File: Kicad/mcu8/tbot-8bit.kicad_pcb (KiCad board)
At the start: 2 copper layers, 80 x 100 mm, 63 parts, among them IC201 TLV1117-50, IC301 PIC16F1778, IC401 MCP2221A, K201 Battery, K301 MCU 1, K302 ICSP, K303 MCU 2, K401 FRONT #1, K402 FRONT #2, K403 VIN, K404 +5V, K405 FRONT #3, K406 SERVO LEFT, K407 USB/UART, K408 SERVO RIGHT, T201 DMP2305U, T202 DMP2305U

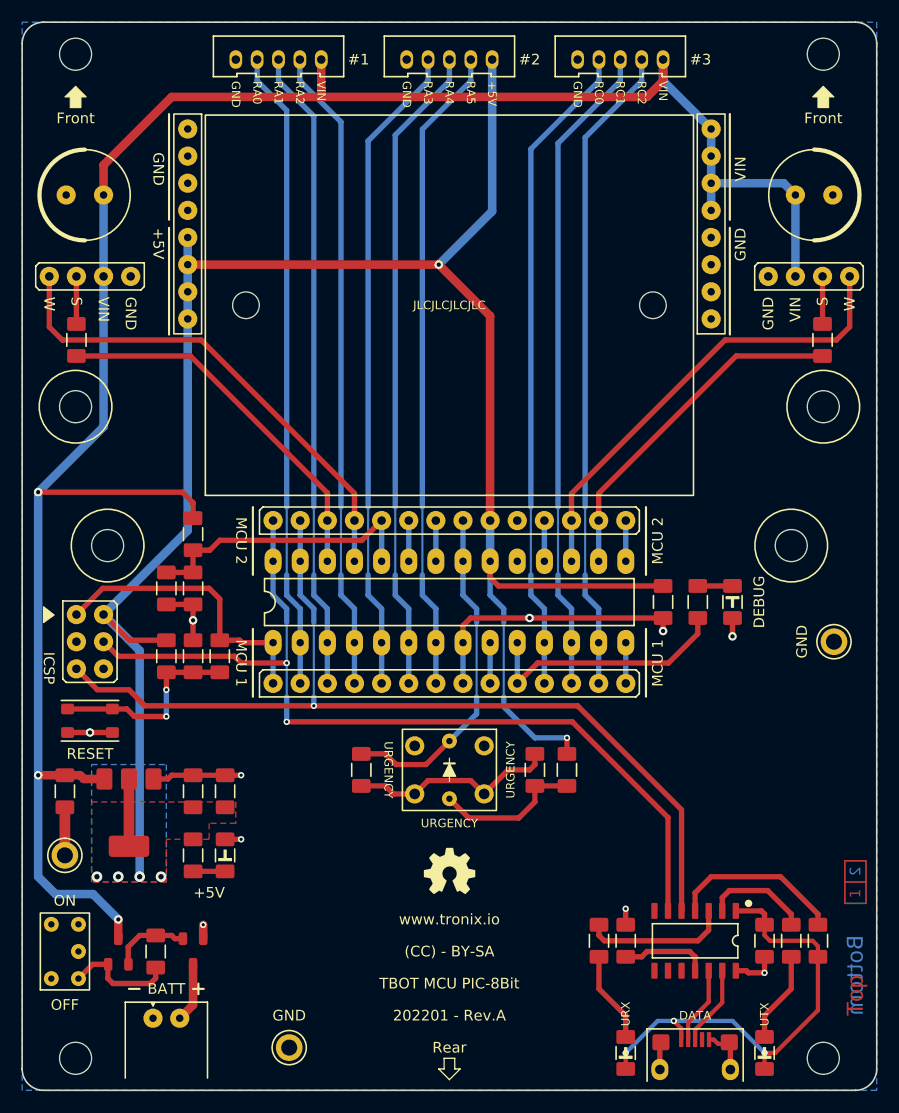
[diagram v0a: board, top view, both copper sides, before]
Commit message: Update MCU 8Bit
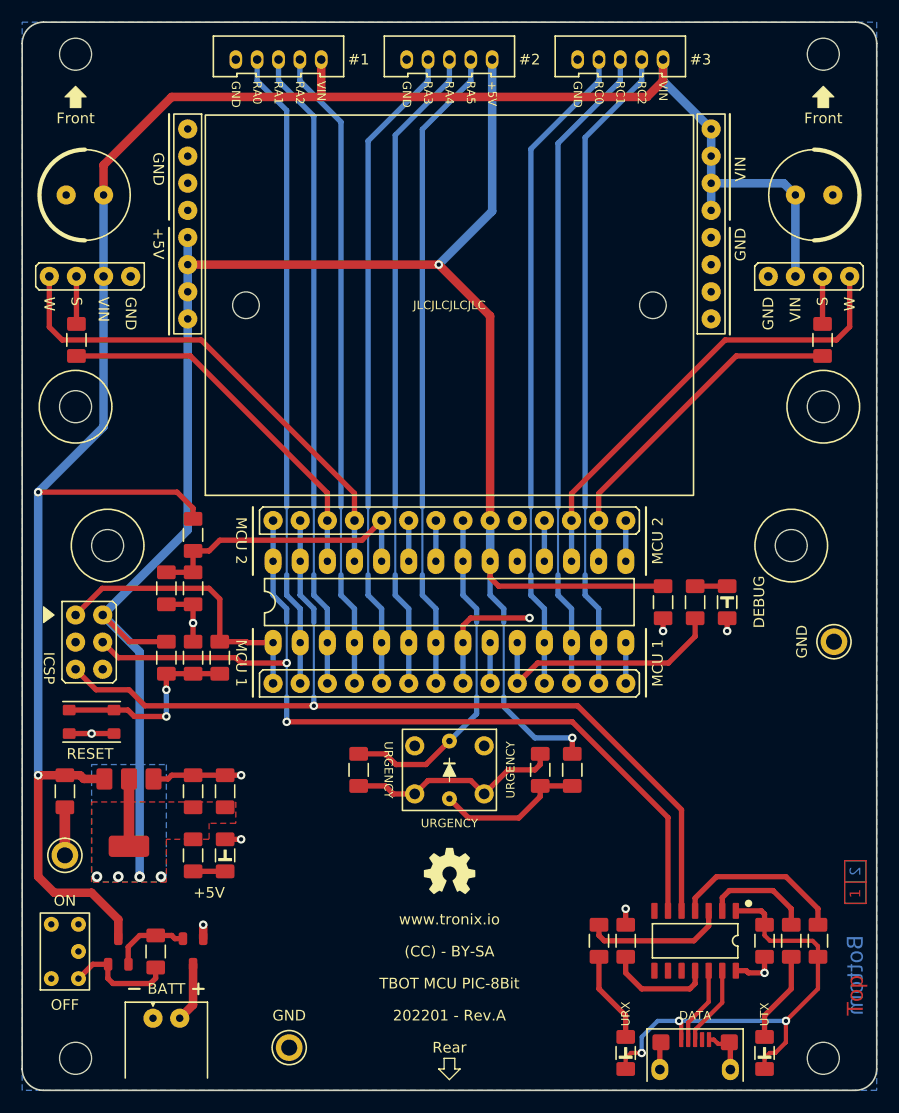
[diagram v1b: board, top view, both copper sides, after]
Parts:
- moved LED401 0.50 mm to (166.0, 104.3)
- moved R401 0.50 mm to (151.5, 120.0)
- moved R402 0.50 mm to (148.5, 120.0)
- moved R404 0.25 mm to (163.0, 104.3)
- moved R403 0.25 mm to (131.5, 120.0)
- moved S301 0.18 mm to (106.5, 115.5)
- moved C301 0.14 mm to (116.0, 109.5)
- moved R301 0.14 mm to (113.5, 109.5)
- moved R302 0.14 mm to (118.5, 109.5)
- moved K302 0.09 mm to (105.0, 105.5)
- moved R203 0.07 mm to (116.0, 98.0)
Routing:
- net GND: track 65.5 -> 52.6 mm
- net Net-(C402-Pad1): track 8.21 -> 10.0 mm
- net Net-(R402-Pad1): track 19.5 -> 20.5 mm
- net VUSB: track 43.4 -> 44.3 mm
- net +5V: track 193.0 -> 193.7 mm
- net /HID/RB0/EMERGENCY: track 31.5 -> 32.0 mm
- net VIN: track 195.9 -> 195.7 mm, vias 3 -> 2

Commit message: Update MCU 8Bit
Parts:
- removed BB401: BREADBOARD-170, tronixio:BREADBOARD-170
- removed C203: 10µ, tronixio:CAPACITOR-1206
- removed C204, C403: 100n, tronixio:CAPACITOR-1206
- removed C401, C404: 220µ/25V, tronixio:CAPACITOR-ELECTROLYTIC-RADIAL-080-115-035
- removed C402: 470n, tronixio:CAPACITOR-1206
- removed IC401: MCP2221A, tronixio:SOIC-SL-14
- removed K401: FRONT #1, tronixio:MOLEX-532530570
- removed K402: FRONT #2, tronixio:MOLEX-532530570
- removed K403: VIN, tronixio:HARWIN-M20-782084x
- removed K404: +5V, tronixio:HARWIN-M20-782084x
- removed K405: FRONT #3, tronixio:MOLEX-532530570
- removed K406: SERVO LEFT, tronixio:HARWIN-M20-999044x
- removed K407: USB/UART, tronixio:FCI-USB-TYPE-B-MICRO-THT
- removed K408: SERVO RIGHT, tronixio:HARWIN-M20-999044x
- removed LED201: Power, tronixio:LED-1206
- removed LED401: Debug, tronixio:LED-1206
- removed LED402: URX, tronixio:LED-1206
- removed LED403: UTX, tronixio:LED-1206
- removed R203: 7K5, tronixio:RESISTOR-1206
- removed R204, R406: 10K, tronixio:RESISTOR-1206
- removed R401, R405, R408: 220Ω, tronixio:RESISTOR-1206
- removed R402: 150Ω, tronixio:RESISTOR-1206
- removed R403: 330Ω, tronixio:RESISTOR-1206
- removed R404, R407, R409: 4K7, tronixio:RESISTOR-1206
- removed S401: EMERGENCY, tronixio:E-SWITCH-TL1240XQ1JXXX
- removed T201, T202: DMP2305U, tronixio:SOT-23-3
- removed TP201, TP202, TP203: GND, tronixio:KEYSTONE-5006
- added BB301: BREADBOARD-170, tronixio:BREADBOARD-170, F.Cu at (140.0, 76.5)
- added C101: 10µ, tronixio:CAPACITOR-1206, F.Cu at (104.0, 122.0)
- added C102: 100n, tronixio:CAPACITOR-1206, F.Cu at (119.0, 122.0)
- added C103: 10µ, tronixio:CAPACITOR-1206, F.Cu at (116.0, 122.0)
- added C104: 100n, tronixio:CAPACITOR-1206, F.Cu at (116.0, 103.0)
- added C303: 100n, tronixio:CAPACITOR-1206, F.Cu at (169.5, 136.0)
- added C304: 220µ/25V, tronixio:CAPACITOR-ELECTROLYTIC-RADIAL-080-115-035, F.Cu at (174.1, 66.2)
- added IC101: TLV1117-50, tronixio:SOT-223-3, F.Cu at (110.0, 124.0)
- added K101: Battery, tronixio:MOLEX-22057025, F.Cu at (112.2, 143.2)
- added K202: ICSP, tronixio:HARWIN-M20-998034x, F.Cu at (105.0, 105.5)
- added K203: MCU 2, tronixio:HARWIN-M20-999144x, F.Cu at (123.5, 96.7)
- added K304: +5V, tronixio:HARWIN-M20-782084x, F.Cu at (115.5, 77.8)
- added K305: FRONT #3, tronixio:MOLEX-532530570, F.Cu at (152.0, 53.5)
- added K306: SERVO LEFT, tronixio:HARWIN-M20-999044x, F.Cu at (110.2, 73.8)
- added K307: USB/UART, tronixio:FCI-USB-TYPE-B-MICRO-THT, F.Cu at (163.0, 147.5)
- added K308: SERVO RIGHT, tronixio:HARWIN-M20-999044x, F.Cu at (169.8, 73.8)
- added LED101: Power, tronixio:LED-1206, F.Cu at (119.0, 128.0)
- added LED301: Debug, tronixio:LED-1206, F.Cu at (166.0, 104.3)
- added LED302: URX, tronixio:LED-1206, F.Cu at (156.5, 146.5)
- added LED303: UTX, tronixio:LED-1206, F.Cu at (169.5, 146.5)
- added R101: 1M, tronixio:RESISTOR-1206, F.Cu at (112.5, 137.0)
- added R102: 4K7, tronixio:RESISTOR-1206, F.Cu at (116.0, 128.0)
- added R103: 7K5, tronixio:RESISTOR-1206, F.Cu at (116.0, 98.0)
- added R104: 10K, tronixio:RESISTOR-1206, F.Cu at (113.5, 103.0)
- added R303: 330Ω, tronixio:RESISTOR-1206, F.Cu at (131.5, 120.0)
- added R304: 4K7, tronixio:RESISTOR-1206, F.Cu at (163.0, 104.3)
- added R305: 220Ω, tronixio:RESISTOR-1206, F.Cu at (105.1, 79.8)
- added R306: 10K, tronixio:RESISTOR-1206, F.Cu at (174.5, 136.0)
- added R307: 4K7, tronixio:RESISTOR-1206, F.Cu at (154.0, 136.0)
- added R308: 220Ω, tronixio:RESISTOR-1206, F.Cu at (174.9, 79.8)
- added R309: 4K7, tronixio:RESISTOR-1206, F.Cu at (172.0, 136.0)
- added S101: Power, tronixio:E-SWITCH-200USPXT1A1M2RE, F.Cu at (104.0, 137.0)
- added T101: DMP2305U, tronixio:SOT-23-3, F.Cu at (116.0, 137.0)
- added T102: DMP2305U, tronixio:SOT-23-3, F.Cu at (109.0, 137.0)
- added TP101: GND, tronixio:KEYSTONE-5006, F.Cu at (104.0, 128.0)
- added TP102: GND, tronixio:KEYSTONE-5006, F.Cu at (125.0, 146.0)
- added TP103: GND, tronixio:KEYSTONE-5006, F.Cu at (176.0, 108.0)
- C201: value 10µ -> 100n
- C301: value 100n -> 220µ/25V; footprint tronixio:CAPACITOR-1206 -> tronixio:CAPACITOR-ELECTROLYTIC-RADIAL-080-115-035
- C302: value 100n -> 470n
- IC201: value TLV1117-50 -> PIC16F1778; footprint tronixio:SOT-223-3 -> tronixio:DIP-28-W762-SOCKET
- IC301: value PIC16F1778 -> MCP2221A; footprint tronixio:DIP-28-W762-SOCKET -> tronixio:SOIC-SL-14
- K201: value Battery -> MCU 1; footprint tronixio:MOLEX-22057025 -> tronixio:HARWIN-M20-999144x
- K301: value MCU 1 -> FRONT #1; footprint tronixio:HARWIN-M20-999144x -> tronixio:MOLEX-532530570
- K302: value ICSP -> FRONT #2; footprint tronixio:HARWIN-M20-998034x -> tronixio:MOLEX-532530570
- K303: value MCU 2 -> VIN; footprint tronixio:HARWIN-M20-999144x -> tronixio:HARWIN-M20-782084x
- R201: value 1M -> 10K
- R202: value 4K7 -> 1K
- R301: value 10K -> 220Ω
- R302: value 1K -> 150Ω
- S201: value Power -> Reset; footprint tronixio:E-SWITCH-200USPXT1A1M2RE -> tronixio:ALPS-SKRPAC
- S301: value Reset -> EMERGENCY; footprint tronixio:ALPS-SKRPAC -> tronixio:E-SWITCH-TL1240XQ1JXXX
- moved K302 60.5 mm to (136.0, 53.5)
- moved K301 58.5 mm to (120.0, 53.5), turned to 0 degrees
- moved K303 55.0 mm to (164.5, 60.0), turned to 0 degrees
- moved IC301 48.4 mm to (163.0, 136.0), turned to -90 degrees
- moved C202 47.4 mm to (160.0, 104.3), turned to -90 degrees
- moved C301 44.5 mm to (105.9, 66.2), turned to 180 degrees
- moved R301 39.4 mm to (151.5, 120.0)
- moved S301 33.8 mm to (140.0, 120.0), turned to 180 degrees
- moved K201 33.3 mm to (123.5, 111.9), turned to 90 degrees
- moved C302 31.9 mm to (156.5, 136.0), turned to 90 degrees
- moved R302 31.8 mm to (148.5, 120.0)
- moved R201 27.5 mm to (113.5, 109.5)
- moved S201 21.6 mm to (106.5, 115.5)
- moved IC201 20.9 mm to (123.5, 108.1), turned to 90 degrees
- moved R202 18.7 mm to (118.5, 109.5), turned to -90 degrees
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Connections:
- C201 pad 1: VIN -> Net-(C201-Pad1)
- C301 pad 1: Net-(C301-Pad1) -> VIN
- C302 pad 1: +5V -> Net-(C302-Pad1)
- IC201 pad 1: GND -> ~{MCLR}
- IC201 pad 2: +5V -> /HID/RA0
- IC201 pad 3: VIN -> /HID/RA1
- IC301 pad 1: ~{MCLR} -> VUSB
- IC301 pad 10: /HID/RA6/LED -> unconnected-(IC301-Pad10)
- IC301 pad 11: /HID/RC0 -> Net-(C302-Pad1)
- IC301 pad 12: /HID/RC1 -> /HID/D-
- IC301 pad 13: /HID/RC2 -> /HID/D+
- IC301 pad 14: RC3 -> GND
- IC301 pad 2: /HID/RA0 -> Net-(IC301-Pad2)
- IC301 pad 3: /HID/RA1 -> Net-(IC301-Pad3)
- IC301 pad 4: /HID/RA2 -> Net-(IC301-Pad4)
- IC301 pad 5: /HID/RA3 -> /HID/RB6/PGC/UTX
- IC301 pad 6: /HID/RA4 -> /HID/RB7/PGD/URX
- IC301 pad 7: /HID/RA5 -> unconnected-(IC301-Pad7)
- IC301 pad 8: GND -> unconnected-(IC301-Pad8)
- IC301 pad 9: RA7 -> unconnected-(IC301-Pad9)
- K201 pad 1: GND -> ~{MCLR}
- K201 pad 2: VBAT -> /HID/RA0
- K301 pad 1: ~{MCLR} -> VIN
- K301 pad 2: /HID/RA0 -> /HID/RA2
- K301 pad 4: /HID/RA2 -> /HID/RA0
- K301 pad 5: /HID/RA3 -> GND
- K302 pad 1: ~{MCLR} -> +5V
- K302 pad 2: +5V -> /HID/RA5
- K302 pad 3: GND -> /HID/RA4
- K302 pad 4: /HID/RB7/PGD/URX -> /HID/RA3
- K302 pad 5: /HID/RB6/PGC/UTX -> GND
- K303 pad 1: /HID/RB7/PGD/URX -> VIN
- K303 pad 2: /HID/RB6/PGC/UTX -> VIN
- K303 pad 3: /HID/RB5/SERVO_L -> VIN
- K303 pad 4: /HID/RB4/WHEEL_L -> VIN
- K303 pad 5: /MCU/RB3/BATTERY_SENSE -> GND
- K303 pad 6: RB2 -> GND
- K303 pad 7: RB1 -> GND
- K303 pad 8: /HID/RB0/EMERGENCY -> GND
- R201 pad 1: Net-(R201-Pad1) -> Net-(C201-Pad1)
- R201 pad 2: Net-(R201-Pad2) -> +5V
- R202 pad 1: Net-(LED201-Pad2) -> ~{MCLR}
- R202 pad 2: +5V -> Net-(C201-Pad1)
- R301 pad 1: Net-(C301-Pad1) -> Net-(R301-Pad1)
- R302 pad 1: ~{MCLR} -> Net-(R302-Pad1)
- R302 pad 2: Net-(C301-Pad1) -> Net-(R301-Pad1)
- S201 pad 1: unconnected-(S201-Pad1) -> GND
- S201 pad 3: Net-(R201-Pad1) -> Net-(C201-Pad1)
- S201 pad 4: (no net) -> Net-(C201-Pad1)
- S301 pad 3: Net-(C301-Pad1) -> Net-(R302-Pad1)
- S301 pad 4: Net-(C301-Pad1) -> Net-(R302-Pad1)
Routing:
- net RB3/BATTERY_SENSE: track 0.00 -> 27.1 mm
- net /MCU/RB3/BATTERY_SENSE: track 27.1 -> 0.00 mm
- net Net-(R402-Pad1): track 20.5 -> 0.00 mm
- net Net-(R302-Pad1): track 0.00 -> 20.5 mm
- net Net-(C301-Pad1): track 18.3 -> 0.00 mm, vias 2 -> 0
- net Net-(C201-Pad1): track 0.00 -> 18.3 mm, vias 0 -> 2
- net Net-(IC401-Pad4): track 16.3 -> 0.00 mm
- net Net-(IC301-Pad4): track 0.00 -> 16.3 mm
- net Net-(R401-Pad1): track 14.1 -> 0.00 mm
- net Net-(R301-Pad1): track 0.00 -> 14.1 mm
- net Net-(IC401-Pad3): track 13.5 -> 0.00 mm
- net Net-(IC301-Pad3): track 0.00 -> 13.5 mm
- net Net-(R201-Pad1): track 10.5 -> 0.00 mm
- net Net-(R101-Pad1): track 0.00 -> 10.5 mm
- net Net-(IC401-Pad2): track 10.2 -> 0.00 mm
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
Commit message: Update tbot-8bit.kicad_pcb
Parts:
- removed TP103: GND, tronixio:KEYSTONE-5006
- moved TP102 54.4 mm to (176.0, 127.0)
- moved TP101 28.0 mm to (125.0, 146.5), turned to 90 degrees
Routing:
- net GND: track 52.6 -> 50.1 mm, vias 10 -> 11
- net VIN: track 195.7 -> 193.6 mm

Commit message: Update tbot-8bit.kicad_pcb
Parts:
- turned LED302 to 90 degrees
- turned LED303 to 90 degrees
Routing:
- net VUSB: track 44.3 -> 37.6 mm
- net Net-(LED302-Pad1): track 8.54 -> 12.4 mm
- net Net-(LED303-Pad1): track 8.54 -> 12.3 mm
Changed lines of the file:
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@@
   )
   (footprint "tronixio:LED-1206" (layer "F.Cu")
-    (at 156.5 146.5 -90)
+    (at 156.5 146.5 90)
     (property "MOUSER" "604-APT3216LSECKJ3RV")
     (property "Sheetfile" "hid.kicad_sch")
@@
     (fp_rect (start -1.5 0.8) (end -1.2 -0.8) (layer "F.Fab") (width 0.1) (fill solid))
     (fp_rect (start -1.2 0.8) (end 1.2 -0.8) (layer "F.Fab") (width 0.1) (fill none))
-    (pad "1" smd roundrect (at -1.5 0 270) (size 1.3 1.75) (layers "F.Cu" "F.Paste" "F.Mask") (roundrect_rratio 0.15)
+    (pad "1" smd roundrect (at -1.5 0 90) (size 1.3 1.75) (layers "F.Cu" "F.Paste" "F.Mask") (roundrect_rratio 0.15)
       (net 52 "Net-(LED302-Pad1)") (pinfunction "K") (pintype "passive") (zone_connect 2))
-    (pad "2" smd roundrect (at 1.5 0 270) (size 1.3 1.75) (layers "F.Cu" "F.Paste" "F.Mask") (roundrect_rratio 0.15)
+    (pad "2" smd roundrect (at 1.5 0 90) (size 1.3 1.75) (layers "F.Cu" "F.Paste" "F.Mask") (roundrect_rratio 0.15)
       (net 4 "VUSB") (pinfunction "A") (pintype "passive") (zone_connect 2))
     (model "${KICAD6_USER_3DMODEL_DIR}/SMD/LED-1206.wrl"
@@
   )
   (footprint "tronixio:LED-1206" (layer "F.Cu")
-    (at 169.5 146.5 -90)
+    (at 169.5 146.5 90)
     (property "MOUSER" "604-APT3216LSECKJ3RV")
     (property "Sheetfile" "hid.kicad_sch")
@@
     (fp_rect (start -1.5 0.8) (end -1.2 -0.8) (layer "F.Fab") (width 0.1) (fill solid))
     (fp_rect (start -1.2 0.8) (end 1.2 -0.8) (layer "F.Fab") (width 0.1) (fill none))
-    (pad "1" smd roundrect (at -1.5 0 270) (size 1.3 1.75) (layers "F.Cu" "F.Paste" "F.Mask") (roundrect_rratio 0.15)
+    (pad "1" smd roundrect (at -1.5 0 90) (size 1.3 1.75) (layers "F.Cu" "F.Paste" "F.Mask") (roundrect_rratio 0.15)
       (net 53 "Net-(LED303-Pad1)") (pinfunction "K") (pintype "passive") (zone_connect 2))
-    (pad "2" smd roundrect (at 1.5 0 270) (size 1.3 1.75) (layers "F.Cu" "F.Paste" "F.Mask") (roundrect_rratio 0.15)
+    (pad "2" smd roundrect (at 1.5 0 90) (size 1.3 1.75) (layers "F.Cu" "F.Paste" "F.Mask") (roundrect_rratio 0.15)
       (net 4 "VUSB") (pinfunction "A") (pintype "passive") (zone_connect 2))
     (model "${KICAD6_USER_3DMODEL_DIR}/SMD/LED-1206.wrl"
@@
   (segment (start 118.5 104) (end 118.5 107.86) (width 0.5) (layer "F.Cu") (net 3))
   (segment (start 123.49 108.09) (end 123.49 111.9) (width 0.5) (layer "B.Cu") (net 3))
-  (segment (start 158 146.5) (end 157 146.5) (width 0.4) (layer "F.Cu") (net 4))
+  (segment (start 169.5 144) (end 169 143.5) (width 0.5) (layer "F.Cu") (net 4))
+  (segment (start 169 143.5) (end 168 143.5) (width 0.5) (layer "F.Cu") (net 4))
+  (segment (start 156.5 144) (end 157 143.5) (width 0.5) (layer "F.Cu") (net 4))
   (segment (start 169.2 133.2) (end 169.5 133.5) (width 0.5) (layer "F.Cu") (net 4))
-  (segment (start 156.5 147) (end 156.5 148) (width 0.4) (layer "F.Cu") (net 4))
-  (segment (start 170.5 146.5) (end 170 146.5) (width 0.4) (layer "F.Cu") (net 4))
-  (segment (start 157 146.5) (end 156.5 147) (width 0.4) (layer "F.Cu") (net 4))
   (segment (start 166.81 133.2) (end 169.2 133.2) (width 0.5) (layer "F.Cu") (net 4))
-  (segment (start 169.5 147) (end 169.5 148) (width 0.4) (layer "F.Cu") (net 4))
   (segment (start 169.5 133.5) (end 169.5 134.5) (width 0.5) (layer "F.Cu") (net 4))
   (segment (start 161.5 143.5) (end 161.7 143.7) (width 0.4) (layer "F.Cu") (net 4))
-  (segment (start 174.5 137.5) (end 174.5 136.5) (width 0.4) (layer "F.Cu") (net 4))
-  (segment (start 171.5 143.5) (end 174.5 140.5) (width 0.4) (layer "F.Cu") (net 4))
-  (segment (start 174.5 136.5) (end 174 136) (width 0.4) (layer "F.Cu") (net 4))
-  (segment (start 169.5 135.5) (end 169.5 134.5) (width 0.4) (layer "F.Cu") (net 4))
-  (segment (start 174 136) (end 170 136) (width 0.4) (layer "F.Cu") (net 4))
-  (segment (start 171.5 145.5) (end 170.5 146.5) (width 0.4) (layer "F.Cu") (net 4))
-  (segment (start 174.5 140.5) (end 174.5 137.5) (width 0.4) (layer "F.Cu") (net 4))
-  (segment (start 171.5 143.5) (end 171.5 145.5) (width 0.4) (layer "F.Cu") (net 4))
+  (segment (start 174.5 137.5) (end 174.5 136.5) (width 0.5) (layer "F.Cu") (net 4))
+  (segment (start 156.5 145) (end 156.5 144) (width 0.5) (layer "F.Cu") (net 4))
+  (segment (start 174.5 136.5) (end 174 136) (width 0.5) (layer "F.Cu") (net 4))
+  (segment (start 169.5 135.5) (end 169.5 134.5) (width 0.5) (layer "F.Cu") (net 4))
+  (segment (start 174 136) (end 170 136) (width 0.5) (layer "F.Cu") (net 4))
+  (segment (start 169.5 145) (end 169.5 144) (width 0.5) (layer "F.Cu") (net 4))
+  (segment (start 157 143.5) (end 161.5 143.5) (width 0.5) (layer "F.Cu") (net 4))
   (segment (start 161.7 143.7) (end 161.7 145.25) (width 0.4) (layer "F.Cu") (net 4))
-  (segment (start 170 146.5) (end 169.5 147) (width 0.4) (layer "F.Cu") (net 4))
-  (segment (start 170 136) (end 169.5 135.5) (width 0.4) (layer "F.Cu") (net 4))
+  (segment (start 170 136) (end 169.5 135.5) (width 0.5) (layer "F.Cu") (net 4))
+  (via (at 172 136) (size 0.6) (drill 0.3) (layers "F.Cu" "B.Cu") (net 4))
   (via (at 161.5 143.5) (size 0.8) (drill 0.4) (layers "F.Cu" "B.Cu") (net 4))
-  (via (at 158 146.5) (size 0.8) (drill 0.4) (layers "F.Cu" "B.Cu") (net 4))
-  (via (at 171.5 143.5) (size 0.8) (drill 0.4) (layers "F.Cu" "B.Cu") (net 4))
-  (segment (start 159.5 143.5) (end 161.5 143.5) (width 0.4) (layer "B.Cu") (net 4))
-  (segment (start 158 146.5) (end 158 145) (width 0.4) (layer "B.Cu") (net 4))
-  (segment (start 158 145) (end 159.5 143.5) (width 0.4) (layer "B.Cu") (net 4))
-  (segment (start 171.5 143.5) (end 161.5 143.5) (width 0.4) (layer "B.Cu") (net 4))
+  (via (at 168 143.5) (size 0.8) (drill 0.4) (layers "F.Cu" "B.Cu") (net 4))
+  (segment (start 168 143.5) (end 172 139.5) (width 0.5) (layer "B.Cu") (net 4))
+  (segment (start 172 139.5) (end 172 136) (width 0.5) (layer "B.Cu") (net 4))
+  (segment (start 161.5 143.5) (end 168 143.5) (width 0.5) (layer "B.Cu") (net 4))
   (segment (start 116 142) (end 116 138.2) (width 0.8) (layer "F.Cu") (net 5))
   (segment (start 114.75 143.25) (end 116 142) (width 0.8) (layer "F.Cu") (net 5))
@@
   (segment (start 162.35 143.65) (end 164.27 141.73) (width 0.4) (layer "F.Cu") (net 17))
   (segment (start 164.27 141.73) (end 164.27 138.8) (width 0.4) (layer "F.Cu") (net 17))
-  (segment (start 163 144.325) (end 165.54 141.785) (width 0.4) (layer "F.Cu") (net 18))
-  (segment (start 163 145.25) (end 163 144.325) (width 0.4) (layer "F.Cu") (net 18))
-  (segment (start 165.54 141.785) (end 165.54 138.8) (width 0.4) (layer "F.Cu") (net 18))
+  (segment (start 165.54 141.6225) (end 165.54 138.8) (width 0.4) (layer "F.Cu") (net 18))
+  (segment (start 163 145.25) (end 163 144.1625) (width 0.4) (layer "F.Cu") (net 18))
+  (segment (start 163 144.1625) (end 165.54 141.6225) (width 0.4) (layer "F.Cu") (net 18))
   (segment (start 152.705 60.795) (end 158 55.5) (width 0.5) (layer "B.Cu") (net 19))
   (segment (start 152.705 103.645) (end 152.705 101.74) (width 0.5) (layer "B.Cu") (net 19))
@@
   (segment (start 165 130) (end 171.5 130) (width 0.5) (layer "F.Cu") (net 46))
   (segment (start 174.5 133) (end 174.5 134.5) (width 0.5) (layer "F.Cu") (net 46))
-  (segment (start 154 140.5) (end 156.5 143) (width 0.5) (layer "F.Cu") (net 52))
-  (segment (start 154 137.5) (end 154 140.5) (width 0.5) (layer "F.Cu") (net 52))
-  (segment (start 156.5 143) (end 156.5 145) (width 0.5) (layer "F.Cu") (net 52))
-  (segment (start 169.5 143) (end 169.5 145) (width 0.5) (layer "F.Cu") (net 53))
-  (segment (start 172 140.5) (end 169.5 143) (width 0.5) (layer "F.Cu") (net 53))
-  (segment (start 172 137.5) (end 172 140.5) (width 0.5) (layer "F.Cu") (net 53))
+  (segment (start 154 147) (end 155 148) (width 0.5) (layer "F.Cu") (net 52))
+  (segment (start 154 137.5) (end 154 147) (width 0.5) (layer "F.Cu") (net 52))
+  (segment (start 155 148) (end 156.5 148) (width 0.5) (layer "F.Cu") (net 52))
+  (segment (start 170.75 148) (end 171.25 147.5) (width 0.5) (layer "F.Cu") (net 53))
+  (segment (start 169.5 148) (end 170.75 148) (width 0.5) (layer "F.Cu") (net 53))
+  (segment (start 172 144.5) (end 172 137.5) (width 0.5) (layer "F.Cu") (net 53))
+  (segment (start 171.25 147.5) (end 171.25 145.25) (width 0.5) (layer "F.Cu") (net 53))
+  (segment (start 171.25 145.25) (end 172 144.5) (width 0.5) (layer "F.Cu") (net 53))
   (segment (start 163 138.8) (end 163 140) (width 0.5) (layer "F.Cu") (net 54))
   (segment (start 158 140.5) (end 156.5 139) (width 0.5) (layer "F.Cu") (net 54))
